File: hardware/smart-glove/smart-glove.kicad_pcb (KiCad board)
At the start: 2 copper layers, 95 x 72 mm, 34 parts, among them J1 USB-C, J2 FLEX, J3 LiPo, SW1 BOOT, SW2 EN, U1 ESP32-WROOM-32E, U2 TP4056, U3 AMS1117-3.3, U4 MPU-6050

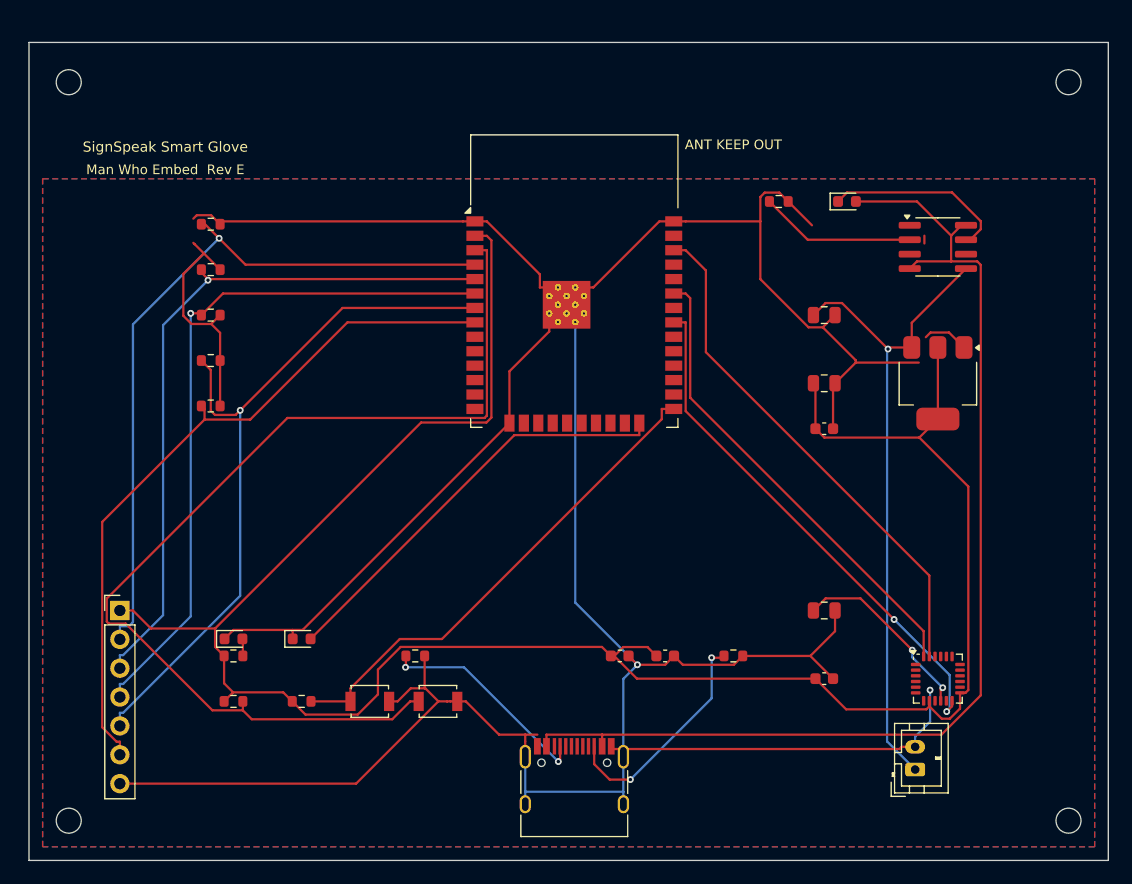
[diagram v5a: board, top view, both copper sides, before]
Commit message: Rev F: 75×52 mm SignSpeak glove-back PCB, DRC gate PASS
Shrink from 95×72 to a dorsal-glove outline with horizontal 1×7 flex
header, cleared H4/J3 hole clearance, and refreshed Gerbers/BOM/CPL.

Co-authored-by: ADIL ZAHOOR  <adilzahoor2812@users.noreply.github.com>
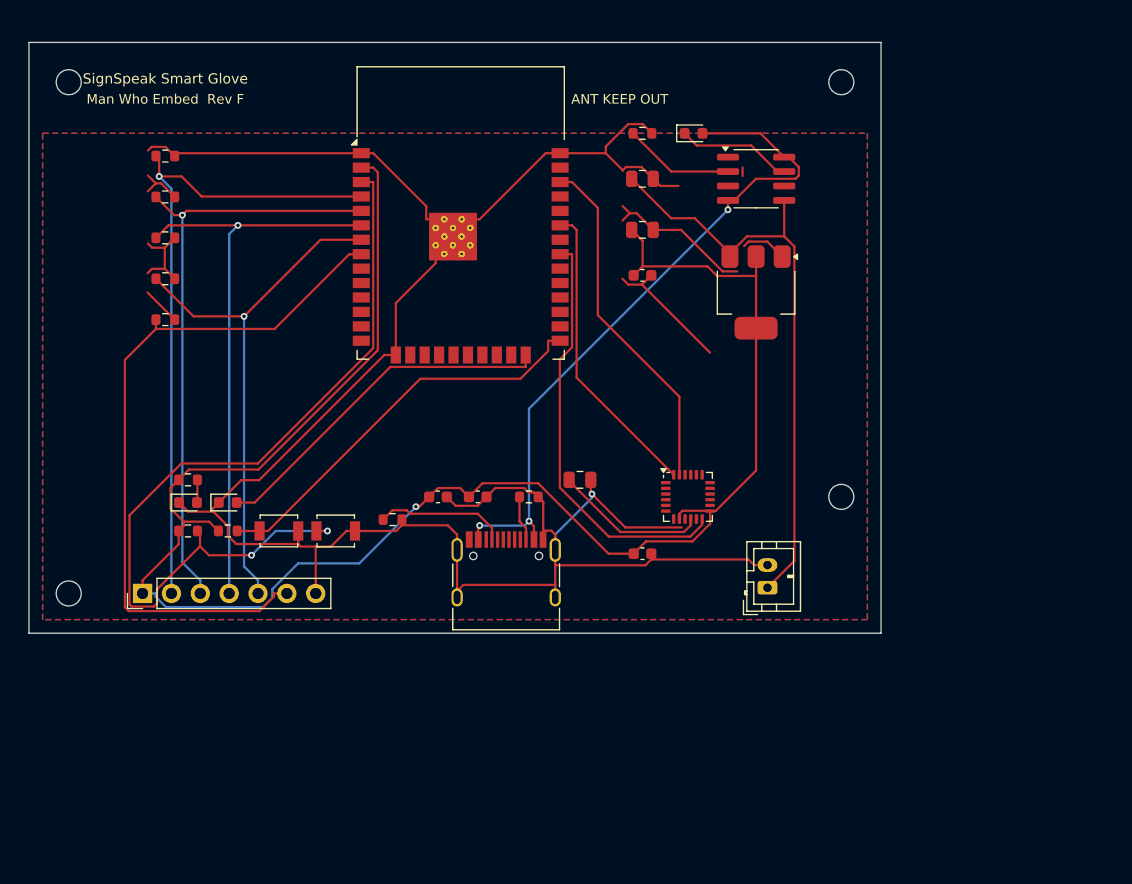
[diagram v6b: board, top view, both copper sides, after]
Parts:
- moved H4 34.8 mm to (71.5, 40.0)
- moved U4 27.2 mm to (58.0, 40.0)
- moved C10 24.4 mm to (48.5, 38.5)
- moved R7 22.8 mm to (44.0, 40.0)
- moved C2 21.6 mm to (39.5, 40.0)
- moved C1 21.3 mm to (36.0, 40.0)
- moved C6 20.9 mm to (54.0, 16.5)
- moved C7 20.9 mm to (54.0, 20.5)
- moved J3 20.6 mm to (65.0, 48.0)
- moved C5 20.0 mm to (54.0, 12.0)
- moved H2 20.0 mm to (71.5, 3.50)
- moved H3 20.0 mm to (3.50, 48.5)
- moved C9 19.4 mm to (54.0, 45.0)
- moved J1 19.2 mm to (42.0, 47.8)
- moved U3 17.9 mm to (64.0, 22.0)
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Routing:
- net GND: track 343.7 -> 253.6 mm, vias 2 -> 1
- net +5V: track 99.8 -> 60.7 mm, vias 0 -> 3
- net 3V3: track 190.6 -> 158.9 mm, vias 0 -> 1
- net FLEX4: track 64.4 -> 47.1 mm
- net CC2: track 20.2 -> 3.99 mm, vias 2 -> 0
- net EN: track 90.2 -> 75.1 mm, vias 0 -> 2
- net SCL: track 45.7 -> 30.7 mm
- net SDA: track 41.7 -> 26.7 mm
- net FLEX3: track 62.4 -> 51.3 mm
- net FLEX2: track 62.2 -> 52.8 mm
- net IMU_INT: track 46.2 -> 37.3 mm, vias 2 -> 0
- net BOOT: track 43.8 -> 35.9 mm
- net CC1: track 19.3 -> 11.6 mm, vias 2 -> 0
- net FLEX1: track 64.9 -> 57.6 mm
- net CHRG: track 16.3 -> 10.2 mm
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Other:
- board size 95 x 72 mm -> 75 x 52 mm
- board text added: "Man Who Embed Rev F"
- board text removed: "Man Who Embed Rev E"

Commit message: Rev G: add UART prog header J4, shrink board to 60×45 mm
40×30 mm is not feasible with ESP32-WROOM-32E + USB-C + charger/IMU.
J4 1×4 (3V3/TX/RX/GND) enables USB-UART dongle flashing. DRC gate PASS.

Co-authored-by: ADIL ZAHOOR  <adilzahoor2812@users.noreply.github.com>
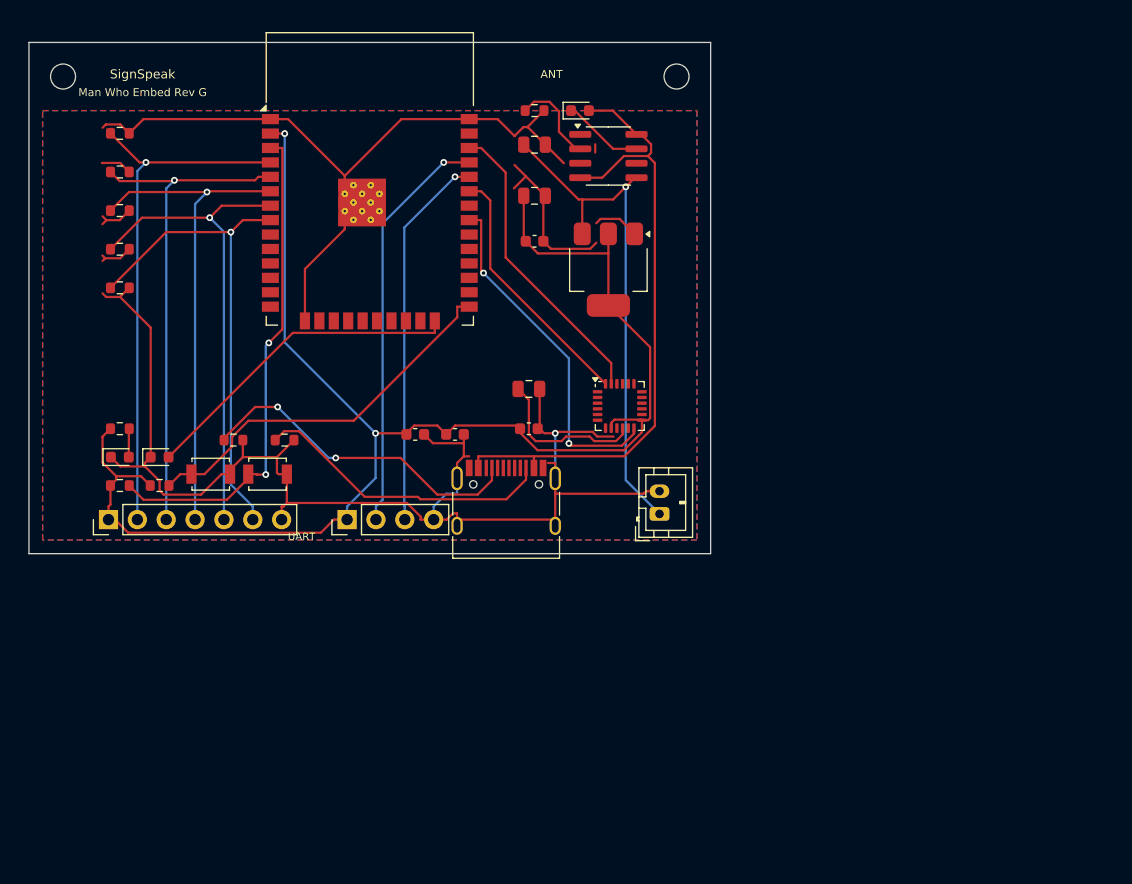
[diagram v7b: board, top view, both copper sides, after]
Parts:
- removed H3, H4: M2, MountingHole_2.2mm_M2
- added J4: UART, PinHeader_1x04_P2.54mm_Vertical, F.Cu at (28.0, 42.0)
- moved R7 22.1 mm to (22.5, 35.0)
- moved R6 15.7 mm to (18.0, 35.0)
- moved C9 14.9 mm to (44.0, 34.0)
- moved H2 14.5 mm to (57.0, 3.00)
- moved U2 13.2 mm to (51.0, 10.0)
- moved U3 13.2 mm to (51.0, 20.0)
- moved J3 11.5 mm to (55.5, 41.5)
- moved D2 10.2 mm to (48.5, 6.00)
- moved U4 10.0 mm to (52.0, 32.0)
- moved C5 9.96 mm to (44.5, 9.00)
- moved C6 9.96 mm to (44.5, 13.5)
- moved C7 9.96 mm to (44.5, 17.5)
- moved R8 9.71 mm to (44.5, 6.00)
- moved C10 9.18 mm to (44.0, 30.5)
- moved U1 8.54 mm to (30.0, 15.0)
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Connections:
- U1 pad 34: (no net) -> UART_RX
- U1 pad 35: (no net) -> UART_TX
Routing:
- net UART_TX: track 0.00 -> 36.2 mm, vias 0 -> 1
- net UART_RX: track 0.00 -> 33.3 mm, vias 0 -> 1
- net GND: track 253.6 -> 222.3 mm
- net EN: track 75.1 -> 44.3 mm
- net 3V3: track 158.9 -> 135.1 mm, vias 1 -> 2
- net CC2: track 3.99 -> 26.6 mm
- net FLEX5: track 62.5 -> 42.6 mm, vias 0 -> 1
- net CC1: track 11.6 -> 29.7 mm, vias 0 -> 2
- net FLEX1: track 57.6 -> 46.9 mm
- net FLEX2: track 52.8 -> 44.7 mm
- net FLEX3: track 51.3 -> 44.0 mm
- net +BAT: track 52.5 -> 45.8 mm, vias 0 -> 1
- net IMU_INT: track 37.3 -> 30.6 mm, vias 0 -> 2
- net FLEX4: track 47.1 -> 42.8 mm
- net SDA: track 26.7 -> 22.5 mm
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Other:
- board size 75 x 52 mm -> 60 x 45 mm
- board text added: "ANT"
- board text added: "Man Who Embed Rev G"
- board text added: "SignSpeak"
- board text added: "UART"
- board text removed: "ANT KEEP OUT"
- board text removed: "Man Who Embed Rev F"
- board text removed: "SignSpeak Smart Glove"
